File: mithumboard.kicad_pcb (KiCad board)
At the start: 2 copper layers, 105 x 57 mm, 32 parts, among them J1 AudioJack4, J2 AudioJack4, J3 AudioJack4, J4 AudioJack4, SW1 SW_Push, SW10 SW_Push, SW11 SW_Push, SW12 SW_Push, SW13 SW_Push, SW14 SW_Push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

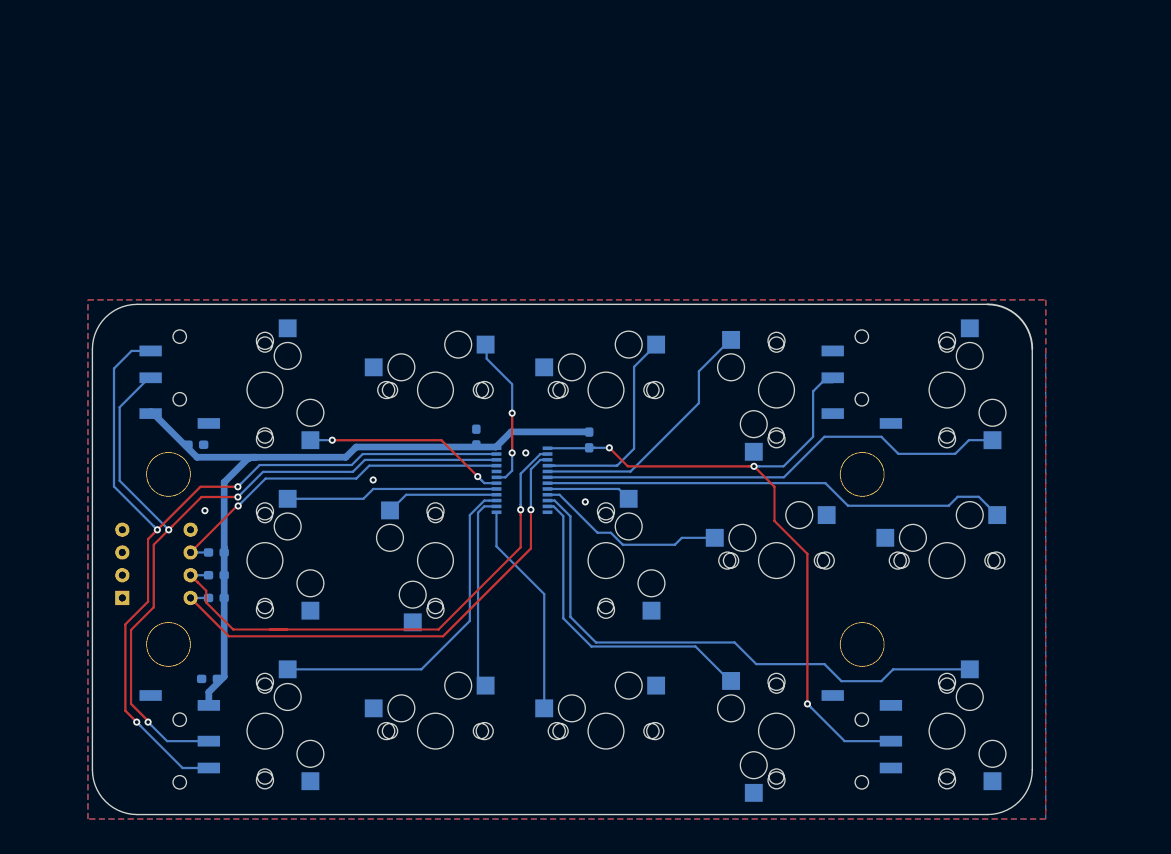
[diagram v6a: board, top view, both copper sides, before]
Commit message: キースイッチの向きを統一
するためにジャックの向きを変更し、キースイッチ群の外に移動。
……上の隙間はなくしたかったんだけれど、あきらめるか……
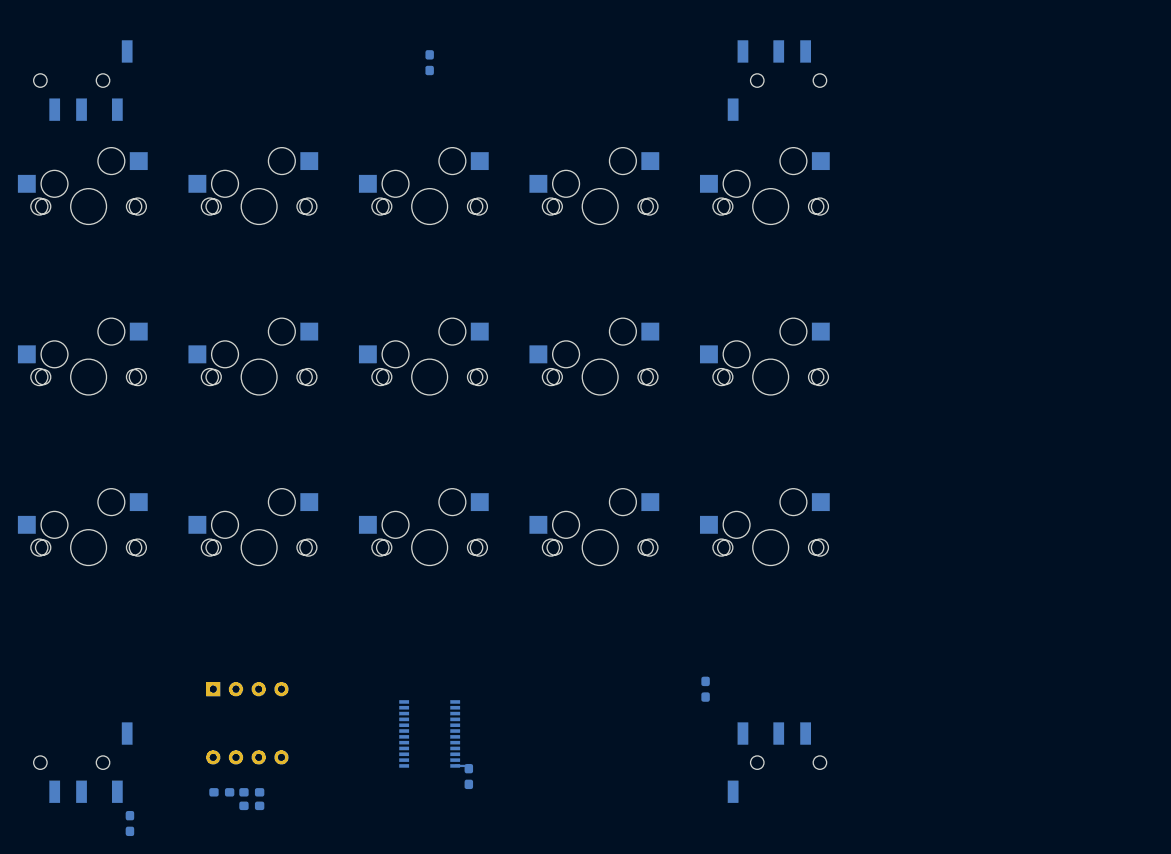
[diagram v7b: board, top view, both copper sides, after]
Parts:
- removed Ref** (x4): Val**, kbd:HOLE
- moved J4 114.0 mm to (50.5, 47.0), turned to 0 degrees
- moved J1 79.3 mm to (128.0, 123.2), turned to 180 degrees
- moved C2 63.2 mm to (120.0, 115.0), turned to 90 degrees
- moved R4 45.8 mm to (89.2, 45.0), turned to 90 degrees
- moved C1 37.9 mm to (93.5, 124.8), turned to 90 degrees
- moved J3 34.7 mm to (128.0, 47.0), turned to 180 degrees
- moved U1 30.2 mm to (89.2, 120.0), turned to 0 degrees
- moved SW1 28.4 mm to (51.1, 61.1), turned to 0 degrees
- moved SW2 28.4 mm to (51.1, 80.1), turned to 0 degrees
- moved SW3 28.4 mm to (51.1, 99.2), turned to 0 degrees
- moved SW4 28.4 mm to (70.1, 61.1)
- moved SW5 28.4 mm to (70.1, 80.1), turned to 0 degrees
- moved SW6 28.4 mm to (70.1, 99.2)
- moved SW7 28.4 mm to (89.2, 61.1)
- moved SW8 28.4 mm to (89.2, 80.1), turned to 0 degrees
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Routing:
- net SDA: track 100.0 -> 0.00 mm, vias 3 -> 0
- net SCL: track 91.6 -> 0.00 mm, vias 3 -> 0
- net INT: track 81.0 -> 0.00 mm, vias 3 -> 0
- net 3.3V: track 82.3 -> 1.53 mm
- net R3C5: track 62.7 -> 0.00 mm
- net A1: track 59.8 -> 0.00 mm, vias 1 -> 0
- net A2: track 57.0 -> 0.00 mm, vias 1 -> 0
- net R1C5: track 53.2 -> 0.00 mm
- net R2C5: track 52.8 -> 0.00 mm
- net A0: track 40.2 -> 0.00 mm, vias 1 -> 0
- net R3C1: track 38.1 -> 0.00 mm
- net R3C4: track 35.9 -> 0.00 mm
- net R1C4: track 28.5 -> 0.00 mm
- net R1C3: track 24.2 -> 0.00 mm
- net R3C3: track 24.1 -> 0.00 mm
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- removed copper zone on B.Cu, net GND
- removed copper zone on F.Cu, net GND
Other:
- board outline removed
- rule pad_to_mask_clearance: 0.051 -> 0
- board text removed: "mithumboard Designed by mitaroThanken"

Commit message: 再配置完了？
穴あけがまだ。
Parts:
- C1, C2, C3: footprint Capacitor_SMD:C_0603_1608Metric_Pad1.05x0.95mm_HandSolder -> Capacitor_THT:C_Disc_D6.0mm_W4.4mm_P5.00mm
- J1, J2, J3, J4: value AudioJack4 -> MJ-4PP-9; footprint Connector_Audio_Mod:Jack_3.5mm_PJ320D_Horizontal_Mod -> kbd:MJ-4PP-9_1side
- R1, R2, R3, R4: footprint Resistor_SMD:R_0603_1608Metric_Pad1.05x0.95mm_HandSolder -> Keebio-Parts:Resistor-Hybrid; moved to F.Cu
- SW1, SW10, SW11, SW12, SW13, SW14, SW15, SW2, SW3, SW4, SW5, SW6, SW7, SW8, SW9: footprint kbd:CherryMX_Hotswap_1side -> kbd:CherryMX_Choc_Hotswap_1side
- moved R3 40.6 mm to (106.6, 124.6)
- moved J1 36.3 mm to (164.3, 123.3), turned to 90 degrees
- moved J3 36.3 mm to (164.3, 47.1), turned to 90 degrees
- moved SW16 32.7 mm to (97.6, 111.5)
- moved C2 30.5 mm to (149.9, 121.2)
- moved C1 29.8 mm to (123.3, 124.2)
- moved U1 28.5 mm to (117.3, 115.4)
- moved SW1 28.1 mm to (79.1, 59.1)
- moved SW13 28.1 mm to (155.3, 59.1)
- moved SW14 28.1 mm to (155.3, 78.1)
- moved SW15 28.1 mm to (155.3, 97.2)
- moved SW2 28.1 mm to (79.1, 78.1)
- moved SW3 28.1 mm to (79.1, 97.2)
- moved SW4 28.1 mm to (98.1, 59.1)
- moved SW5 28.1 mm to (98.1, 78.1)
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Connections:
- SW10 pad 1: GND -> R1C4
- SW10 pad 2: R1C4 -> GND
- SW12 pad 1: GND -> R3C4
- SW12 pad 2: R3C4 -> GND
- SW13 pad 1: GND -> R1C5
- SW13 pad 2: R1C5 -> GND
- SW14 pad 1: GND -> R2C5
- SW14 pad 2: R2C5 -> GND
- SW2 pad 1: R2C1 -> GND
- SW2 pad 2: GND -> R2C1
- SW3 pad 1: R3C1 -> GND
- SW3 pad 2: GND -> R3C1
- SW4 pad 1: GND -> R1C2
- SW4 pad 2: R1C2 -> GND
- SW5 pad 1: GND -> R2C2
- SW5 pad 2: R2C2 -> GND
- SW7 pad 1: GND -> R1C3
- SW7 pad 2: R1C3 -> GND
- SW9 pad 1: R3C3 -> GND
- SW9 pad 2: GND -> R3C3
- U1 pad 10: R3C5 -> R1C3
- U1 pad 11: R3C4 -> R2C3
- U1 pad 14: R3C2 -> R1C4
- U1 pad 15: R3C1 -> R2C4
- U1 pad 16: R2C2 -> R3C4
- U1 pad 17: R2C1 -> R1C5
- U1 pad 18: R1C1 -> R2C5
- U1 pad 19: R1C2 -> R3C5
- U1 pad 4: R1C3 -> R3C1
- U1 pad 5: R1C4 -> R2C1
- U1 pad 6: R1C5 -> R1C1
- U1 pad 7: R2C5 -> R1C2
- U1 pad 8: R2C3 -> R2C2
- U1 pad 9: R2C4 -> R3C2
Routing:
- net INT: track 0.00 -> 165.8 mm
- net 3.3V: track 1.53 -> 157.3 mm
- net SDA: track 0.00 -> 98.3 mm, vias 0 -> 2
- net SCL: track 0.00 -> 91.8 mm, vias 0 -> 2
- net R1C1: track 0.00 -> 86.0 mm
- net R1C2: track 0.00 -> 80.3 mm
- net R1C5: track 0.00 -> 77.2 mm, vias 0 -> 2
- net R2C1: track 0.00 -> 67.6 mm
- net R1C3: track 0.00 -> 63.0 mm
- net R1C4: track 0.00 -> 60.1 mm, vias 0 -> 2
- net R2C5: track 0.00 -> 59.2 mm, vias 0 -> 2
- net R2C2: track 0.00 -> 56.5 mm
- net R3C1: track 0.00 -> 50.6 mm
- net R2C3: track 0.00 -> 42.1 mm, vias 0 -> 2
- net R2C4: track 0.00 -> 41.7 mm, vias 0 -> 2
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- added copper zone on B.Cu, net GND
- added copper zone on F.Cu, net GND
